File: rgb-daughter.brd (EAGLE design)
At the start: 226.1 x 74 mm, 100 parts

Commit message: 💄 adding logo
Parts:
- moved FRAME1 54.5 mm to (178.7, 41.3), flipped to the bottom
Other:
- board text added: "Louis Orleans"
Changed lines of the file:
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@@
 <layer number="28" name="bValues" color="7" fill="1" visible="yes" active="yes"/>
 <layer number="29" name="tStop" color="7" fill="3" visible="no" active="yes"/>
-<layer number="30" name="bStop" color="7" fill="6" visible="no" active="yes"/>
+<layer number="30" name="bStop" color="7" fill="6" visible="yes" active="yes"/>
 <layer number="31" name="tCream" color="7" fill="4" visible="no" active="yes"/>
 <layer number="32" name="bCream" color="7" fill="5" visible="no" active="yes"/>
@@
 <wire x1="111.369646875" y1="39.584096875" x2="114.8697875" y2="39.584096875" width="0.0508" layer="20"/>
 <wire x1="111.369646875" y1="34.583903125" x2="114.8697875" y2="34.583903125" width="0.0508" layer="20"/>
+<text x="152.019" y="41.275" size="1.6764" layer="22" font="vector" rot="MR0">Louis Orleans</text>
+<circle x="189.23" y="36.83" radius="7.62" width="0.1524" layer="30"/>
+<circle x="189.23" y="36.83" radius="6.731" width="1.016" layer="30"/>
+<wire x1="191.262" y1="33.02" x2="191.262" y2="36.195" width="1.27" layer="30"/>
+<wire x1="191.262" y1="36.195" x2="191.262" y2="40.64" width="1.27" layer="30"/>
+<wire x1="188.468" y1="40.64" x2="188.468" y2="36.195" width="1.27" layer="30" curve="180"/>
+<wire x1="191.262" y1="40.64" x2="188.468" y2="40.64" width="1.27" layer="30"/>
+<wire x1="188.468" y1="36.195" x2="191.262" y2="36.195" width="1.27" layer="30"/>
+<wire x1="191.262" y1="33.02" x2="186.436" y2="33.02" width="1.27" layer="30"/>
+<polygon width="0.0762" layer="22">
+<vertex x="186.182" y="40.132"/>
+<vertex x="183.007" y="36.957"/>
+<vertex x="183.007" y="36.83" curve="90"/>
+<vertex x="189.23" y="30.607"/>
+<vertex x="189.738" y="30.607"/>
+<vertex x="191.643" y="32.512"/>
+<vertex x="191.389" y="32.385"/>
+<vertex x="186.436" y="32.385" curve="-180"/>
+<vertex x="186.436" y="33.655"/>
+<vertex x="190.627" y="33.655"/>
+<vertex x="190.627" y="35.56"/>
+<vertex x="188.468" y="35.56" curve="-126.869898"/>
+</polygon>
+<polygon width="0.0762" layer="22">
+<vertex x="190.627" y="40.005"/>
+<vertex x="190.627" y="36.83"/>
+<vertex x="188.468" y="36.83" curve="-180"/>
+<vertex x="188.468" y="40.005"/>
+</polygon>
+<polygon width="0.0762" layer="22">
+<vertex x="184.15" y="42.037"/>
+<vertex x="182.753" y="40.64"/>
+<vertex x="182.372" y="40.005"/>
+<vertex x="182.118" y="39.243"/>
+<vertex x="181.864" y="38.354"/>
+<vertex x="181.737" y="37.338"/>
+<vertex x="181.737" y="36.195"/>
+<vertex x="181.864" y="35.306"/>
+<vertex x="182.118" y="34.417"/>
+<vertex x="182.499" y="33.401"/>
+<vertex x="183.007" y="32.639"/>
+<vertex x="183.769" y="31.623"/>
+<vertex x="184.531" y="30.988"/>
+<vertex x="185.42" y="30.353"/>
+<vertex x="186.436" y="29.845"/>
+<vertex x="187.325" y="29.591"/>
+<vertex x="188.595" y="29.337"/>
+<vertex x="189.738" y="29.337"/>
+<vertex x="190.627" y="29.464"/>
+<vertex x="191.643" y="29.718"/>
+<vertex x="192.786" y="30.226"/>
+<vertex x="193.04" y="30.353"/>
+<vertex x="194.437" y="31.75"/>
+<vertex x="193.675" y="31.115"/>
+<vertex x="192.913" y="30.607"/>
+<vertex x="191.897" y="30.099"/>
+<vertex x="191.135" y="29.845"/>
+<vertex x="190.627" y="29.718"/>
+<vertex x="189.865" y="29.591"/>
+<vertex x="188.341" y="29.591"/>
+<vertex x="187.325" y="29.845"/>
+<vertex x="186.436" y="30.099"/>
+<vertex x="185.674" y="30.48"/>
+<vertex x="185.039" y="30.861"/>
+<vertex x="184.404" y="31.369"/>
+<vertex x="183.896" y="31.877"/>
+<vertex x="183.388" y="32.512"/>
+<vertex x="182.88" y="33.274"/>
+<vertex x="182.499" y="34.036"/>
+<vertex x="182.245" y="34.925"/>
+<vertex x="182.118" y="35.56"/>
+<vertex x="181.991" y="36.83"/>
+<vertex x="182.118" y="38.227"/>
+<vertex x="182.372" y="39.243"/>
+<vertex x="182.753" y="40.132"/>
+<vertex x="183.261" y="41.021"/>
+<vertex x="183.896" y="41.783"/>
+</polygon>
 </plain>
 <attributes>
@@
 </autorouter>
 <elements>
-<element name="FRAME1" library="SparkFun-Aesthetics" library_urn="urn:adsk.eagle:library:507" package="CREATIVE_COMMONS" package3d_urn="urn:adsk.eagle:package:37121/1" value="FRAME-LETTER" x="157.48" y="-8.89"/>
+<element name="FRAME1" library="SparkFun-Aesthetics" library_urn="urn:adsk.eagle:library:507" package="CREATIVE_COMMONS" package3d_urn="urn:adsk.eagle:package:37121/1" value="FRAME-LETTER" x="178.689" y="41.275" rot="MR0"/>
 <element name="J1" library="SparkFun-Connectors" library_urn="urn:adsk.eagle:library:513" package="1X05_1.27MM" package3d_urn="urn:adsk.eagle:package:38110/1" value="" x="39.1395625" y="47.159578125" rot="R270">
 <attribute name="GND" value="" x="37.930421875" y="46.8865625" size="0.6096" layer="27" font="vector" align="bottom-right" display="name"/>

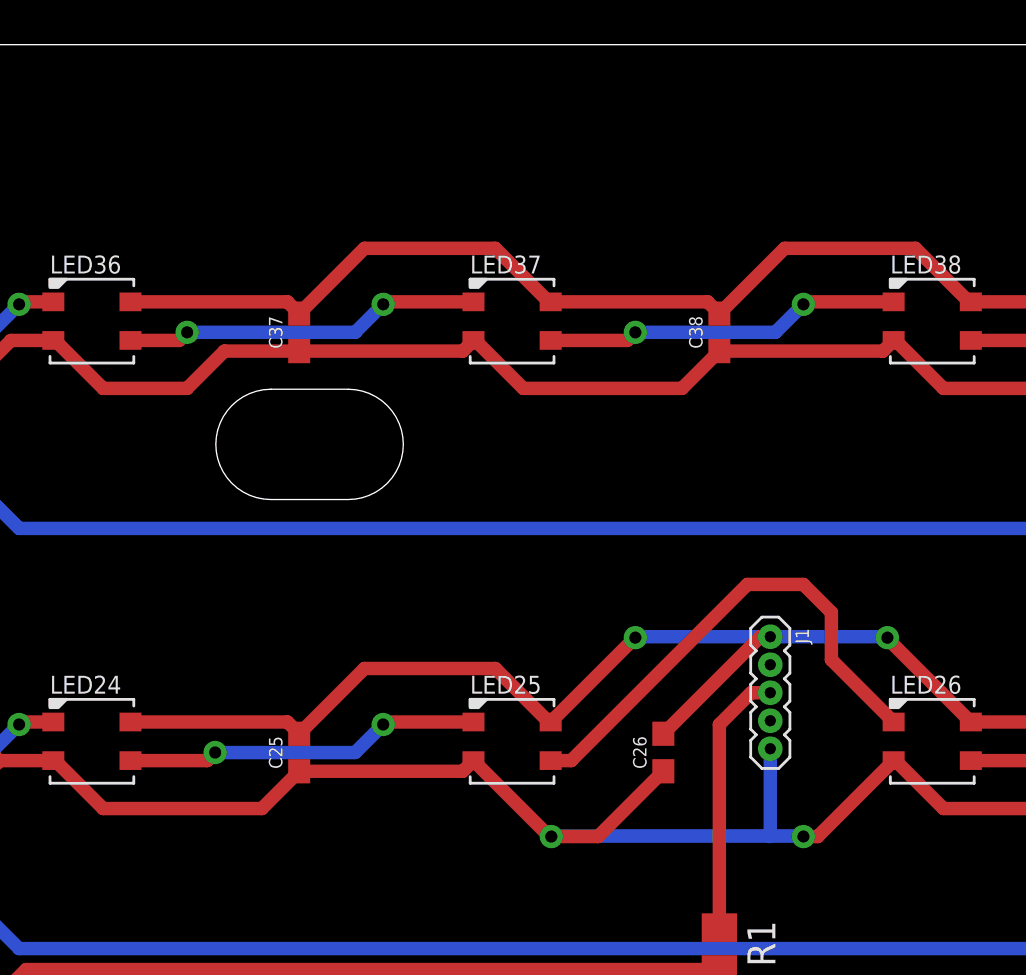
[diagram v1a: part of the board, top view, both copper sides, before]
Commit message: 🚧✨ create USB Type-C part
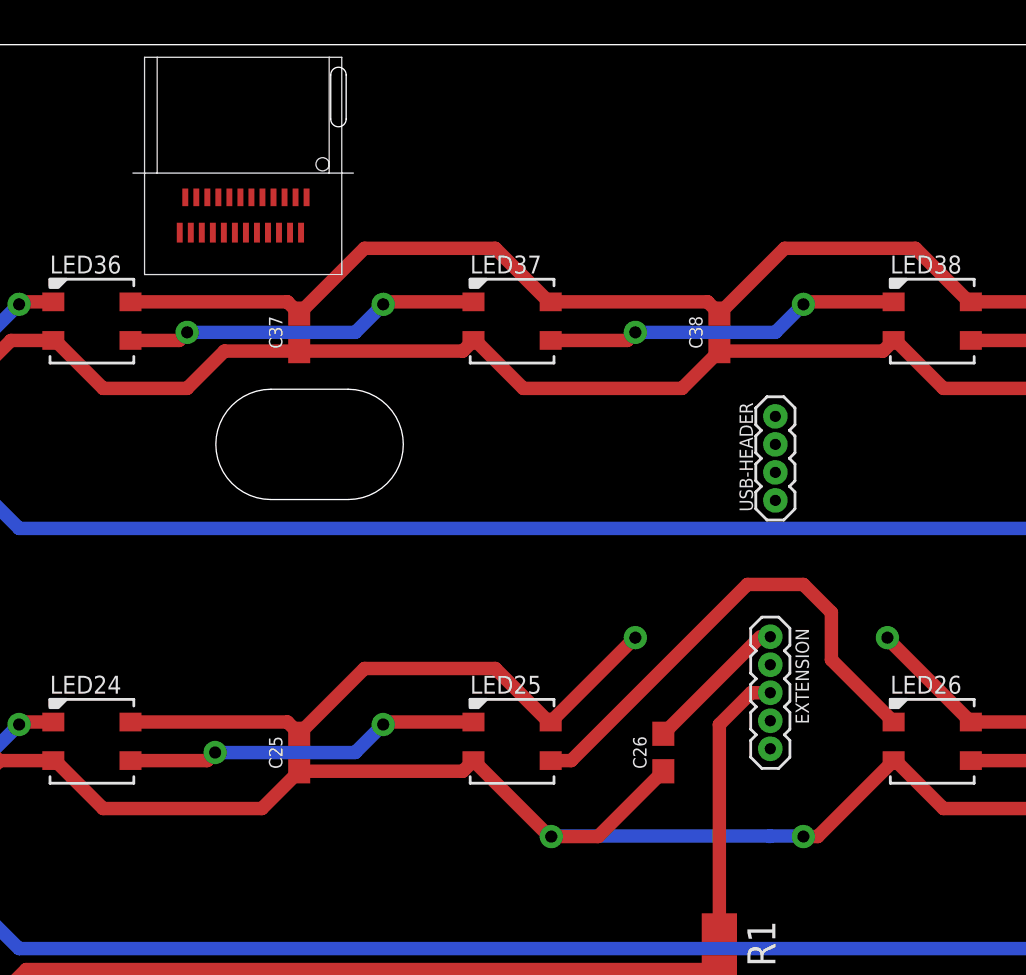
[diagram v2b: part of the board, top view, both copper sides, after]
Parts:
- added FRAME3: FRAME-LETTER, SparkFun-Aesthetics:CREATIVE_COMMONS
- added U$1: USB-TYPE-CDX07S024JJ3R1300, usb:DX07S024JJ3R1300
- added USB-HEADER: (no value), SparkFun-Connectors:1X04_1.27MM
- renumbered J1 to EXTENSION
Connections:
- new net USB-D+: U$1.A6, U$1.B6, USB-HEADER.2
- new net USB-D-: U$1.A7, U$1.B7, USB-HEADER.3
- net GND: now also U$1.A1, U$1.A12, U$1.B1, U$1.B12, USB-HEADER.1
- net VDD: now also U$1.A4, U$1.A9, U$1.B4, U$1.B9, USB-HEADER.4
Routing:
- net GND: track 1023.0 -> 1011.2 mm
- net VDD: track 1044.3 -> 1040.4 mm
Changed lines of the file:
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@@
 <elements>
 <element name="FRAME1" library="SparkFun-Aesthetics" library_urn="urn:adsk.eagle:library:507" package="CREATIVE_COMMONS" package3d_urn="urn:adsk.eagle:package:37121/1" value="FRAME-LETTER" x="178.689" y="41.275" rot="MR0"/>
-<element name="J1" library="SparkFun-Connectors" library_urn="urn:adsk.eagle:library:513" package="1X05_1.27MM" package3d_urn="urn:adsk.eagle:package:38110/1" value="" x="39.1395625" y="47.159578125" rot="R270">
+<element name="EXTENSION" library="SparkFun-Connectors" library_urn="urn:adsk.eagle:library:513" package="1X05_1.27MM" package3d_urn="urn:adsk.eagle:package:38110/1" value="" x="39.1395625" y="47.159578125" rot="R270">
 <attribute name="GND" value="" x="37.930421875" y="46.8865625" size="0.6096" layer="27" font="vector" align="bottom-right" display="name"/>
 <attribute name="PB2" value="" x="37.930421875" y="44.3465625" size="0.6096" layer="27" font="vector" align="bottom-right" display="name"/>
@@
 <attribute name="PROD_ID" value="CAP-00810" x="217.17" y="69.85" size="1.778" layer="27" display="off"/>
 </element>
+<element name="FRAME3" library="SparkFun-Aesthetics" library_urn="urn:adsk.eagle:library:507" package="CREATIVE_COMMONS" package3d_urn="urn:adsk.eagle:package:37121/1" value="FRAME-LETTER" x="10.16" y="-27.94"/>
+<element name="U$1" library="usb" package="DX07S024JJ3R1300" value="USB-TYPE-CDX07S024JJ3R1300" x="15.24" y="68.58" rot="R180"/>
+<element name="USB-HEADER" library="SparkFun-Connectors" library_urn="urn:adsk.eagle:library:513" package="1X04_1.27MM" package3d_urn="urn:adsk.eagle:package:38086/1" value="" x="39.37" y="53.34" rot="R90"/>
 </elements>
 <signals>
 <signal name="GND">
-<contactref element="J1" pad="1"/>
 <contactref element="LED1" pad="4"/>
 <contactref element="C1" pad="2"/>
@@
 <contactref element="LED47" pad="4"/>
 <contactref element="C48" pad="2"/>
-<wire x1="44.407421875" y1="47.159578125" x2="39.1395625" y2="47.159578125" width="0.6096" layer="16"/>
 <wire x1="44.407421875" y1="47.159578125" x2="44.45" y2="47.117" width="0.6096" layer="16"/>
 <via x="44.45" y="47.117" extent="1-16" drill="0.55"/>
 <wire x1="44.45" y1="47.117" x2="44.45" y2="47.075" width="0.6096" layer="1"/>
 <wire x1="44.45" y1="47.075" x2="48.232" y2="43.293" width="0.6096" layer="1"/>
-<wire x1="39.1395625" y1="47.159578125" x2="33.062578125" y2="47.159578125" width="0.6096" layer="16"/>
 <wire x1="33.062578125" y1="47.159578125" x2="33.02" y2="47.117" width="0.6096" layer="16"/>
 <via x="33.02" y="47.117" extent="1-16" drill="0.55"/>
 <wire x1="33.02" y1="47.117" x2="33.006" y2="47.117" width="0.6096" layer="1"/>
 <wire x1="33.006" y1="47.117" x2="29.182" y2="43.293" width="0.6096" layer="1"/>
-<wire x1="39.1395625" y1="47.159578125" x2="38.689578125" y2="47.159578125" width="0.6096" layer="1"/>
 <wire x1="38.689578125" y1="47.159578125" x2="34.29" y2="42.76" width="0.6096" layer="1"/>
 <wire x1="10.132" y1="5.193" x2="17.247" y2="5.193" width="0.6096" layer="1"/>
@@
 <wire x1="218.02" y1="50.8" x2="218.02" y2="60.681" width="0.6096" layer="1"/>
 <wire x1="218.02" y1="60.681" x2="219.682" y2="62.343" width="0.6096" layer="1"/>
+<contactref element="U$1" pad="A1"/>
+<contactref element="U$1" pad="B12"/>
+<contactref element="U$1" pad="A12"/>
+<contactref element="U$1" pad="B1"/>
+<contactref element="USB-HEADER" pad="1"/>
+<contactref element="EXTENSION" pad="1"/>
+<wire x1="39.1395625" y1="47.159578125" x2="39.37" y2="53.34" width="0" layer="19" extent="1-1"/>
+<wire x1="38.689578125" y1="47.159578125" x2="39.1395625" y2="47.159578125" width="0" layer="19" extent="1-1"/>
+<wire x1="33.02" y1="47.117" x2="34.29" y2="42.76" width="0" layer="19" extent="1-16"/>
+<wire x1="44.407421875" y1="47.159578125" x2="39.1395625" y2="47.159578125" width="0" layer="19" extent="16-16"/>
+<wire x1="17.865" y1="65.48" x2="20.74" y2="64.77" width="0" layer="19" extent="1-1"/>
+<wire x1="18.115" y1="67.08" x2="17.865" y2="65.48" width="0" layer="19" extent="1-1"/>
+<wire x1="12.365" y1="65.48" x2="10.132" y2="62.343" width="0" layer="19" extent="1-1"/>
+<wire x1="12.615" y1="67.08" x2="12.365" y2="65.48" width="0" layer="19" extent="1-1"/>
 </signal>
 <signal name="VDD">
-<contactref element="J1" pad="5"/>
 <contactref element="LED1" pad="2"/>
 <contactref element="C1" pad="1"/>
@@
 <contactref element="LED47" pad="2"/>
 <contactref element="C48" pad="1"/>
-<wire x1="39.1395625" y1="42.079578125" x2="39.1395625" y2="38.1235625" width="0.6096" layer="16"/>
 <wire x1="39.1395625" y1="38.1235625" x2="39.116" y2="38.1" width="0.6096" layer="16"/>
 <wire x1="39.1395625" y1="38.1235625" x2="40.6164375" y2="38.1235625" width="0.6096" layer="16"/>
@@
 <wire x1="204.89" y1="22.01" x2="203.2" y2="20.32" width="0.6096" layer="1"/>
 <wire x1="203.2" y1="20.32" x2="199.39" y2="20.32" width="0.6096" layer="1"/>
+<contactref element="U$1" pad="A4"/>
+<contactref element="U$1" pad="B9"/>
+<contactref element="U$1" pad="A9"/>
+<contactref element="U$1" pad="B4"/>
+<contactref element="USB-HEADER" pad="4"/>
+<contactref element="EXTENSION" pad="5"/>
+<wire x1="36.83" y1="60.11" x2="39.37" y2="57.15" width="0" layer="19" extent="1-1"/>
+<wire x1="39.1395625" y1="42.079578125" x2="39.1395625" y2="38.1235625" width="0" layer="19" extent="16-16"/>
+<wire x1="13.865" y1="65.48" x2="14.39" y2="60.11" width="0" layer="19" extent="1-1"/>
+<wire x1="14.115" y1="67.08" x2="13.865" y2="65.48" width="0" layer="19" extent="1-1"/>
+<wire x1="16.615" y1="67.08" x2="14.115" y2="67.08" width="0" layer="19" extent="1-1"/>
+<wire x1="16.365" y1="65.48" x2="16.615" y2="67.08" width="0" layer="19" extent="1-1"/>
 </signal>
 <signal name="N$3">
-<contactref element="J1" pad="3"/>
+<contactref element="EXTENSION" pad="3"/>
 <contactref element="R1" pad="1"/>
 <wire x1="39.1395625" y1="44.619578125" x2="38.269578125" y2="44.619578125" width="0.6096" layer="1"/>
@@
 <wire x1="116.953" y1="5.193" x2="116.84" y2="5.08" width="0.6096" layer="1"/>
 </signal>
+<signal name="USB-D-">
+<contactref element="U$1" pad="B7"/>
+<contactref element="U$1" pad="A7"/>
+<contactref element="USB-HEADER" pad="3"/>
+<wire x1="15.615" y1="67.08" x2="39.37" y2="55.88" width="0" layer="19" extent="1-1"/>
+<wire x1="14.865" y1="65.48" x2="15.615" y2="67.08" width="0" layer="19" extent="1-1"/>
+</signal>
+<signal name="USB-D+">
+<contactref element="U$1" pad="A6"/>
+<contactref element="U$1" pad="B6"/>
+<contactref element="USB-HEADER" pad="2"/>
+<wire x1="15.115" y1="67.08" x2="39.37" y2="54.61" width="0" layer="19" extent="1-1"/>
+<wire x1="15.365" y1="65.48" x2="15.115" y2="67.08" width="0" layer="19" extent="1-1"/>
+</signal>
 </signals>

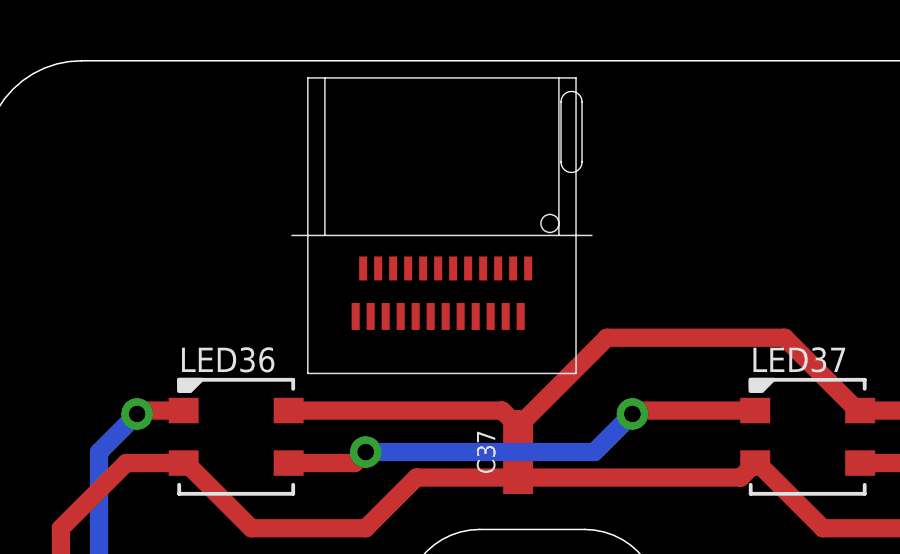
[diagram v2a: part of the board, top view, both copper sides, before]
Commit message: ⬆️ updating USB Type-C package
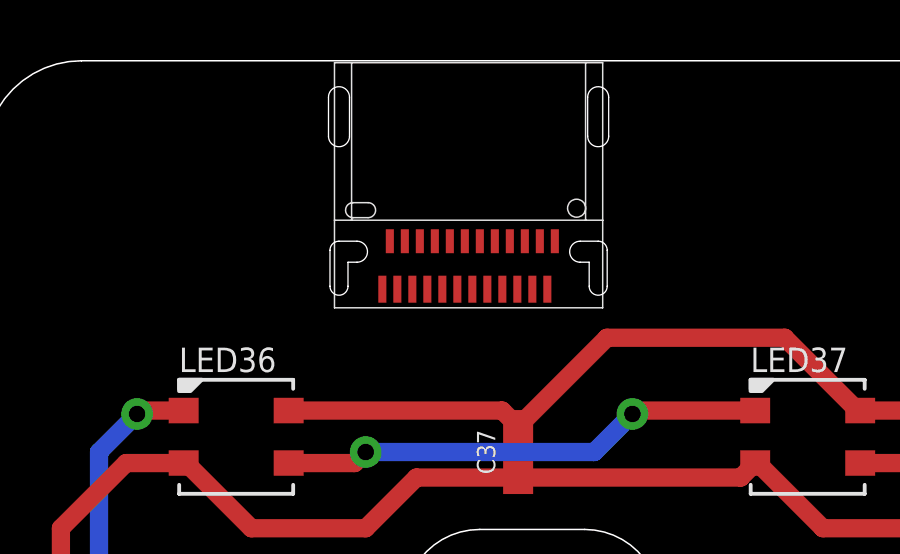
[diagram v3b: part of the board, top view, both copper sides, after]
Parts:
- moved U$1 1.02 mm to (16.1, 69.1)
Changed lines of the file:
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@@
 </element>
 <element name="FRAME3" library="SparkFun-Aesthetics" library_urn="urn:adsk.eagle:library:507" package="CREATIVE_COMMONS" package3d_urn="urn:adsk.eagle:package:37121/1" value="FRAME-LETTER" x="10.16" y="-27.94"/>
-<element name="U$1" library="usb" package="DX07S024JJ3R1300" value="USB-TYPE-CDX07S024JJ3R1300" x="15.24" y="68.58" rot="R180"/>
+<element name="U$1" library="usb" package="DX07S024JJ3R1300" value="USB-TYPE-CDX07S024JJ3R1300" x="16.129" y="69.088" rot="R180"/>
 <element name="USB-HEADER" library="SparkFun-Connectors" library_urn="urn:adsk.eagle:library:513" package="1X04_1.27MM" package3d_urn="urn:adsk.eagle:package:38086/1" value="" x="39.37" y="53.34" rot="R90"/>
 </elements>
@@
 <wire x1="33.02" y1="47.117" x2="34.29" y2="42.76" width="0" layer="19" extent="1-16"/>
 <wire x1="44.407421875" y1="47.159578125" x2="39.1395625" y2="47.159578125" width="0" layer="19" extent="16-16"/>
-<wire x1="17.865" y1="65.48" x2="20.74" y2="64.77" width="0" layer="19" extent="1-1"/>
-<wire x1="18.115" y1="67.08" x2="17.865" y2="65.48" width="0" layer="19" extent="1-1"/>
-<wire x1="12.365" y1="65.48" x2="10.132" y2="62.343" width="0" layer="19" extent="1-1"/>
-<wire x1="12.615" y1="67.08" x2="12.365" y2="65.48" width="0" layer="19" extent="1-1"/>
+<wire x1="18.754" y1="66.388" x2="20.74" y2="64.77" width="0" layer="19" extent="1-1"/>
+<wire x1="19.004" y1="67.988" x2="18.754" y2="66.388" width="0" layer="19" extent="1-1"/>
+<wire x1="13.254" y1="66.388" x2="10.132" y2="62.343" width="0" layer="19" extent="1-1"/>
+<wire x1="13.504" y1="67.988" x2="13.254" y2="66.388" width="0" layer="19" extent="1-1"/>
 </signal>
 <signal name="VDD">
@@
 <wire x1="36.83" y1="60.11" x2="39.37" y2="57.15" width="0" layer="19" extent="1-1"/>
 <wire x1="39.1395625" y1="42.079578125" x2="39.1395625" y2="38.1235625" width="0" layer="19" extent="16-16"/>
-<wire x1="13.865" y1="65.48" x2="14.39" y2="60.11" width="0" layer="19" extent="1-1"/>
-<wire x1="14.115" y1="67.08" x2="13.865" y2="65.48" width="0" layer="19" extent="1-1"/>
-<wire x1="16.615" y1="67.08" x2="14.115" y2="67.08" width="0" layer="19" extent="1-1"/>
-<wire x1="16.365" y1="65.48" x2="16.615" y2="67.08" width="0" layer="19" extent="1-1"/>
+<wire x1="14.754" y1="66.388" x2="14.39" y2="60.11" width="0" layer="19" extent="1-1"/>
+<wire x1="15.004" y1="67.988" x2="14.754" y2="66.388" width="0" layer="19" extent="1-1"/>
+<wire x1="17.504" y1="67.988" x2="15.004" y2="67.988" width="0" layer="19" extent="1-1"/>
+<wire x1="17.254" y1="66.388" x2="17.504" y2="67.988" width="0" layer="19" extent="1-1"/>
 </signal>
 <signal name="N$3">
@@
 <contactref element="U$1" pad="A7"/>
 <contactref element="USB-HEADER" pad="3"/>
-<wire x1="15.615" y1="67.08" x2="39.37" y2="55.88" width="0" layer="19" extent="1-1"/>
-<wire x1="14.865" y1="65.48" x2="15.615" y2="67.08" width="0" layer="19" extent="1-1"/>
+<wire x1="16.504" y1="67.988" x2="39.37" y2="55.88" width="0" layer="19" extent="1-1"/>
+<wire x1="15.754" y1="66.388" x2="16.504" y2="67.988" width="0" layer="19" extent="1-1"/>
 </signal>
 <signal name="USB-D+">
@@
 <contactref element="U$1" pad="B6"/>
 <contactref element="USB-HEADER" pad="2"/>
-<wire x1="15.115" y1="67.08" x2="39.37" y2="54.61" width="0" layer="19" extent="1-1"/>
-<wire x1="15.365" y1="65.48" x2="15.115" y2="67.08" width="0" layer="19" extent="1-1"/>
+<wire x1="16.004" y1="67.988" x2="39.37" y2="54.61" width="0" layer="19" extent="1-1"/>
+<wire x1="16.254" y1="66.388" x2="16.004" y2="67.988" width="0" layer="19" extent="1-1"/>
 </signal>
 </signals>
